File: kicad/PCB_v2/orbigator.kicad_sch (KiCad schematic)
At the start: 47 parts, among them J1 Conn_01x01, J10 Conn_01x01, J11 Conn_01x01, J12 Conn_01x01, J13 Conn_01x01, J14 Conn_01x01, J15 Conn_01x01, J16 Conn_01x01, J17 Conn_01x01, J18 Conn_01x01, J19 Conn_01x01, J2 Conn_01x01, J20 Conn_01x01, J21 Conn_01x01, J22 Conn_01x01, J23 Conn_01x01, J24 Conn_01x01, J25 Conn_01x01, J26 Conn_01x01, J27 Barrel_Jack_Switch, J28 Conn_01x01, J29 Conn_01x01, J3 Conn_01x01, J30 Conn_01x01, J31 Conn_01x01, J32 Conn_01x01, J33 Conn_01x01, J34 Conn_01x01, J35 Conn_01x01, J36 Conn_01x01, J37 Conn_01x01, J4 Conn_01x01, J5 Conn_01x01, J6 Conn_01x01, J7 Conn_01x01, J8 Conn_01x01, J9 Conn_01x01, M1 DYNAMIXEL_1, M2 DYNAMIXEL_2, U1 Pico_2, U2 74LS126, U3 DC_polarity

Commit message: v2 PCB WIP
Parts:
- removed J28, J29, J30: Conn_01x01, orbigator:PinHeader_1x01_P2.54mm_Vertical, symbol orbigator:Conn_01x01_1
- added BT1: CR1220, orbigator:BatteryHolder_LINX_BAT-HLD-012-SMT, symbol orbigator:Battery_Cell
- added C1, C2: 100nF, orbigator:C_0805_2012Metric_Pad1.18x1.45mm_HandSolder, symbol orbigator:C
- added D1: B130, orbigator:D_SMA, symbol orbigator:B130
- added Q1: DMG2305UX, orbigator:SOT-23, symbol orbigator:DMG2305UX
- added R4, R5: 10k, orbigator:R_0805_2012Metric_Pad1.20x1.40mm_HandSolder, symbol orbigator:R
- added U4: DS3232M, orbigator:SOIC-8_3.9x4.9mm_P1.27mm, symbol orbigator:DS3232M
- J27: symbol Connector:Barrel_Jack_Switch -> orbigator:Barrel_Jack_Switch
- R1, R2, R3: footprint orbigator:R_Axial_DIN0207_L6.3mm_D2.5mm_P7.62mm_Horizontal -> orbigator:R_0805_2012Metric_Pad1.20x1.40mm_HandSolder
- RTC1: symbol Connector_Generic:Conn_01x07 -> orbigator:Conn_01x07; GitHub (none) -> https://github.com/process1183/kicad-library; Product URL (none) -> https://www.adafruit.com/product/3013
- U2: footprint orbigator:DIP-14_W7.62mm -> orbigator:SOIC-14_3.9x8.7mm_P1.27mm
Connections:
- net 32k: now also R4.2 (-), U4.1 (32KHZ)
- net 3V3: now also C1.1 (+), R4.1 (+), R5.1 (+), U4.2 (VCC)
- net 5V0: now also D1.2 (A), Q1.3 (D); no longer U1.40 (VBUS)
- net GND: now also BT1.2 (-), C1.2 (-), C2.2 (-), U4.5 (GND)
- net INT: now also R5.2 (-), U4.3 (~{INT}/SQW)
- net RST: now also U4.4 (~{RST})
- net SCL: now also U4.8 (SCL)
- net SDA: now also U4.7 (SDA)
- net 5V_SYS renamed V_SYS
- net V_SYS: now also D1.1 (K), Q1.2 (S)
- new net VBAT: BT1.1 (+), C2.1 (+), U4.6 (VBAT)
- new net V_BUS: Q1.1 (G), U1.40 (VBUS)
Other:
- moved on the sheet: DISP1, J1, J10, J11, J12, J13, J14, J15, J16, J17, J18, J19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

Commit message: v2 PCB WiP
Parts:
- removed J31, J33: Conn_01x01, orbigator:PinHeader_1x01_P2.54mm_Vertical, symbol orbigator:Conn_01x01_1
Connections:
- net 5V0: no longer J25.1 (Pin_1)
- net V_BUS: now also J25.1 (Pin_1)
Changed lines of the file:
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@@
 	)
 	(junction
-		(at 91.44 170.18)
-		(diameter 0)
-		(color 0 0 0 0)
-	)
-	(junction
 		(at 48.26 91.44)
 		(diameter 0)
@@
 	)
 	(junction
-		(at 91.44 165.1)
-		(diameter 0)
-		(color 0 0 0 0)
-	)
-	(junction
 		(at 71.12 41.91)
 		(diameter 0)
@@
 	(wire
 		(pts
-			(xy 91.44 162.56) (xy 91.44 165.1)
+			(xy 91.44 162.56) (xy 91.44 167.64)
 		)
 		(stroke
@@
 	(wire
 		(pts
-			(xy 91.44 170.18) (xy 91.44 172.72)
+			(xy 91.44 167.64) (xy 91.44 172.72)
 		)
 		(stroke
@@
 	(wire
 		(pts
-			(xy 91.44 165.1) (xy 91.44 167.64)
-		)
-		(stroke
-			(width 0)
-			(type default)
-		)
-	)
-	(wire
-		(pts
 			(xy 199.39 111.76) (xy 199.39 114.3)
 		)
@@
 	(wire
 		(pts
-			(xy 91.44 167.64) (xy 91.44 170.18)
-		)
-		(stroke
-			(width 0)
-			(type default)
-		)
-	)
-	(wire
-		(pts
 			(xy 91.44 177.8) (xy 91.44 180.34)
 		)
@@
 		)
 	)
-	(label "5V0"
-		(at 91.44 86.36 0)
-		(effects
-			(font
-				(size 1.27 1.27)
-			)
-			(justify left bottom)
-		)
-	)
 	(label "MOT_DAT"
 		(at 247.65 128.27 180)
@@
 		)
 	)
+	(label "V_BUS"
+		(at 91.44 86.36 0)
+		(effects
+			(font
+				(size 1.27 1.27)
+			)
+			(justify left bottom)
+		)
+	)
 	(label "3V3"
 		(at 181.61 120.65 0)
@@
 	)
 	(symbol
-		(lib_name "Conn_01x01_1")
-		(lib_id "orbigator:Conn_01x01_1")
-		(at 86.36 170.18 180)
-		(unit 1)
-		(exclude_from_sim no)
-		(in_bom yes)
-		(on_board yes)
-		(dnp no)
-		(property "Reference" "J33"
-			(at 82.804 170.18 0)
-			(effects
-				(font
-					(size 1.27 1.27)
-				)
-			)
-		)
-		(property "Value" "Conn_01x01"
-			(at 83.82 168.91 0)
-			(effects
-				(font
-					(size 1.27 1.27)
-				)
-				(justify left)
-				(hide yes)
-			)
-		)
-		(property "Footprint" "orbigator:PinHeader_1x01_P2.54mm_Vertical"
-			(at 86.36 170.18 0)
-			(effects
-				(font
-					(size 1.27 1.27)
-				)
-				(hide yes)
-			)
-		)
-		(property "Datasheet" "~"
-			(at 86.36 170.18 0)
-			(effects
-				(font
-					(size 1.27 1.27)
-				)
-				(hide yes)
-			)
-		)
-		(property "Description" "Generic connector, single row, 01x01, script generated (kicad-library-utils/schlib/autogen/connector/)"
-			(at 86.36 170.18 0)
-			(effects
-				(font
-					(size 1.27 1.27)
-				)
-				(hide yes)
-			)
-		)
-		(pin "1"
-		)
-		(instances
-			(project "orbigator"
-				(path "/3d523963-06e2-453a-8bb2-b2b8ea33bdb6"
-					(reference "J33")
-					(unit 1)
-				)
-			)
-		)
-	)
-	(symbol
 		(lib_name "Conn_01x01_7")
 		(lib_id "orbigator:Conn_01x01_7")
@@
 					(unit 1)
 				)
-			)
-		)
-	)
-	(symbol
-		(lib_name "Conn_01x01_1")
-		(lib_id "orbigator:Conn_01x01_1")
-		(at 86.36 165.1 180)
-		(unit 1)
-		(exclude_from_sim no)
-		(in_bom yes)
-		(on_board yes)
-		(dnp no)
-		(property "Reference" "J31"
-			(at 82.804 165.1 0)
-			(effects
-				(font
-					(size 1.27 1.27)
-				)
-			)
-		)
-		(property "Value" "Conn_01x01"
-			(at 83.82 163.83 0)
-			(effects
-				(font
-					(size 1.27 1.27)
-				)
-				(justify left)
-				(hide yes)
-			)
-		)
-		(property "Footprint" "orbigator:PinHeader_1x01_P2.54mm_Vertical"
-			(at 86.36 165.1 0)
-			(effects
-				(font
-					(size 1.27 1.27)
-				)
-				(hide yes)
-			)
-		)
-		(property "Datasheet" "~"
-			(at 86.36 165.1 0)
-			(effects
-				(font
-					(size 1.27 1.27)
-				)
-				(hide yes)
-			)
-		)
-		(property "Description" "Generic connector, single row, 01x01, script generated (kicad-library-utils/schlib/autogen/connector/)"
-			(at 86.36 165.1 0)
-			(effects
-				(font
-					(size 1.27 1.27)
-				)
-				(hide yes)
-			)
-		)
-		(pin "1"
-		)
-		(instances
-			(project "orbigator"
-				(path "/3d523963-06e2-453a-8bb2-b2b8ea33bdb6"
-					(reference "J31")
-					(unit 1)
-				)

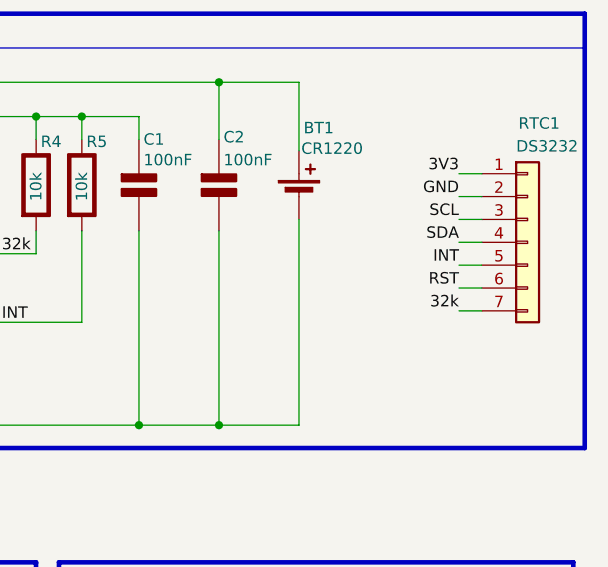
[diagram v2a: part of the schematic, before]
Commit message: orbigator v2 pcb ready for fab
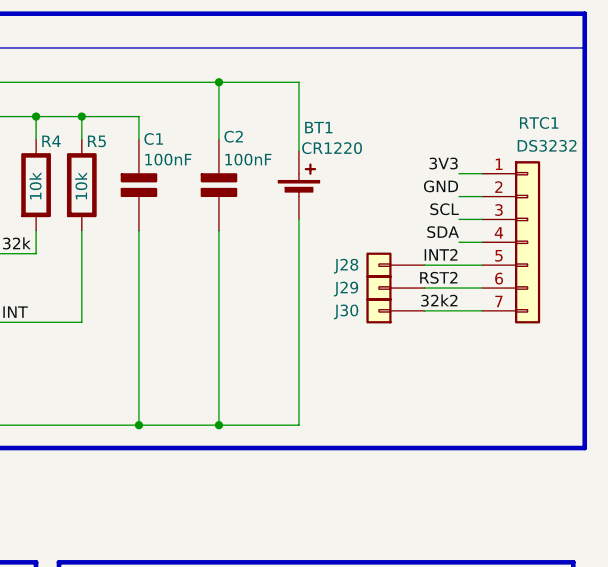
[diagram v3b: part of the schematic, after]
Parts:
- added J28, J29, J30: Conn_01x01, orbigator:PinHeader_1x01_P2.54mm_Vertical, symbol orbigator:Conn_01x01_7
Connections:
- net 32k: no longer RTC1.7 (Pin_7)
- net INT: no longer RTC1.5 (Pin_5)
- net RST: no longer RTC1.6 (Pin_6)
- new net 32k2: J30.1 (Pin_1), RTC1.7 (Pin_7)
- new net INT2: J28.1 (Pin_1), RTC1.5 (Pin_5)
- new net RST2: J29.1 (Pin_1), RTC1.6 (Pin_6)

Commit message: orbigator v2 WIP - not final yet
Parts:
- BT1: footprint orbigator:BatteryHolder_LINX_BAT-HLD-012-SMT -> orbigator:batt_HARWIN_S8201-46R
- DC1: renamed from U3; now not fitted; now left out of the parts list
- J1, RTC1: now left out of the parts list
- J10: footprint orbigator:PinHeader_1x01_P2.54mm_Vertical -> (none); symbol orbigator:Conn_01x01_16 -> orbigator:Conn_01x01; now left out of the parts list
- J11: footprint orbigator:PinHeader_1x01_P2.54mm_Vertical -> (none); symbol orbigator:Conn_01x01_15 -> orbigator:Conn_01x01; now left out of the parts list
- J12: footprint orbigator:PinHeader_1x01_P2.54mm_Vertical -> (none); symbol orbigator:Conn_01x01_14 -> orbigator:Conn_01x01; now left out of the parts list
- J13: footprint orbigator:PinHeader_1x01_P2.54mm_Vertical -> (none); symbol orbigator:Conn_01x01_13 -> orbigator:Conn_01x01; now left out of the parts list
- J14: footprint orbigator:PinHeader_1x01_P2.54mm_Vertical -> (none); symbol orbigator:Conn_01x01_12 -> orbigator:Conn_01x01; now left out of the parts list
- J15: footprint orbigator:PinHeader_1x01_P2.54mm_Vertical -> (none); symbol orbigator:Conn_01x01_11 -> orbigator:Conn_01x01; now left out of the parts list
- J16: footprint orbigator:PinHeader_1x01_P2.54mm_Vertical -> (none); symbol orbigator:Conn_01x01_10 -> orbigator:Conn_01x01; now left out of the parts list
- J17: footprint orbigator:PinHeader_1x01_P2.54mm_Vertical -> (none); symbol orbigator:Conn_01x01_9 -> orbigator:Conn_01x01; now left out of the parts list
- J18: footprint orbigator:PinHeader_1x01_P2.54mm_Vertical -> (none); symbol orbigator:Conn_01x01_8 -> orbigator:Conn_01x01; now left out of the parts list
- J19, J28, J29, J30: footprint orbigator:PinHeader_1x01_P2.54mm_Vertical -> (none); symbol orbigator:Conn_01x01_7 -> orbigator:Conn_01x01; now left out of the parts list
- J2: footprint orbigator:PinHeader_1x01_P2.54mm_Vertical -> (none); symbol orbigator:Conn_01x01_24 -> orbigator:Conn_01x01; now left out of the parts list
- J20: footprint orbigator:PinHeader_1x01_P2.54mm_Vertical -> (none); symbol orbigator:Conn_01x01_6 -> orbigator:Conn_01x01; now left out of the parts list
- J21: footprint orbigator:PinHeader_1x01_P2.54mm_Vertical -> (none); symbol orbigator:Conn_01x01_5 -> orbigator:Conn_01x01; now left out of the parts list
- J22: footprint orbigator:PinHeader_1x01_P2.54mm_Vertical -> (none); symbol orbigator:Conn_01x01_4 -> orbigator:Conn_01x01; now left out of the parts list
- J23: footprint orbigator:PinHeader_1x01_P2.54mm_Vertical -> (none); symbol orbigator:Conn_01x01_3 -> orbigator:Conn_01x01; now left out of the parts list
- J24: footprint orbigator:PinHeader_1x01_P2.54mm_Vertical -> (none); symbol orbigator:Conn_01x01_2 -> orbigator:Conn_01x01; now left out of the parts list
- J25, J26, J32, J34, J35, J36, J37: footprint orbigator:PinHeader_1x01_P2.54mm_Vertical -> (none); symbol orbigator:Conn_01x01_1 -> orbigator:Conn_01x01; now left out of the parts list
- J3: footprint orbigator:PinHeader_1x01_P2.54mm_Vertical -> (none); symbol orbigator:Conn_01x01_23 -> orbigator:Conn_01x01; now left out of the parts list
- J4: footprint orbigator:PinHeader_1x01_P2.54mm_Vertical -> (none); symbol orbigator:Conn_01x01_22 -> orbigator:Conn_01x01; now left out of the parts list
- J5: footprint orbigator:PinHeader_1x01_P2.54mm_Vertical -> (none); symbol orbigator:Conn_01x01_21 -> orbigator:Conn_01x01; now left out of the parts list
- J6: footprint orbigator:PinHeader_1x01_P2.54mm_Vertical -> (none); symbol orbigator:Conn_01x01_20 -> orbigator:Conn_01x01; now left out of the parts list
- J7: footprint orbigator:PinHeader_1x01_P2.54mm_Vertical -> (none); symbol orbigator:Conn_01x01_19 -> orbigator:Conn_01x01; now left out of the parts list
- J8: footprint orbigator:PinHeader_1x01_P2.54mm_Vertical -> (none); symbol orbigator:Conn_01x01_18 -> orbigator:Conn_01x01; now left out of the parts list
- J9: footprint orbigator:PinHeader_1x01_P2.54mm_Vertical -> (none); symbol orbigator:Conn_01x01_17 -> orbigator:Conn_01x01; now left out of the parts list

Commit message: orbigator v2 WIP2 - not final yet
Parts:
- added C3, C5, C6, C7, C9: 100nF, orbigator:C_0805_2012Metric_Pad1.18x1.45mm_HandSolder, symbol orbigator:C
- added C8: 100uF, orbigator:CP_Elec_6.3x9.9, symbol PCM_Elektuur:C-polar
- DC1: now fitted
- J10, J11, J12, J13, J14, J15, J16, J17, J18, J19, J2, J20, J21, J22, J23, J24, J25, J26, J28, J29, J3, J30, J32, J34, J35, J36, J37, J4, J5, J6, J7, J8, J9: footprint (none) -> orbigator:PinHeader_1x01_P2.54mm_Vertical
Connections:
- net 3V3: now also C5.1 (+), C9.1 (+)
- net 5V0: now also C6.1 (+), C7.1 (+), C8.1 (+)
- net GND: now also C3.2 (-), C5.2 (-), C6.2 (-), C7.2 (-), C8.2 (-), C9.2 (-)
- net V_SYS: now also C3.1 (+)
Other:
- moved on the sheet: BT1, C1, C2, D1, DISP1, J27, J28, J29, J30, M1, M2, Q1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
